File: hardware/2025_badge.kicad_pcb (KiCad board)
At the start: 2 copper layers, 83.8 x 138 mm, 233 parts, among them J1 Conn_01x02, J10 Conn_01x02, J11 Conn_01x02, J12 Conn_01x02, J13 Conn_01x02, J14 Conn_01x02, J15 Conn_01x02, J16 Conn_01x02, J2 Conn_01x02, J3 Conn_01x02, J4 Conn_01x02, J5 Conn_01x02, J6 Conn_01x02, J7 Conn_01x02, J8 Conn_01x02, J9 Conn_01x02, Q1 2N7000, SW1 SW_SPDT, SW2 SW_Push, SW3 SW_Push, U1 TSOP4838

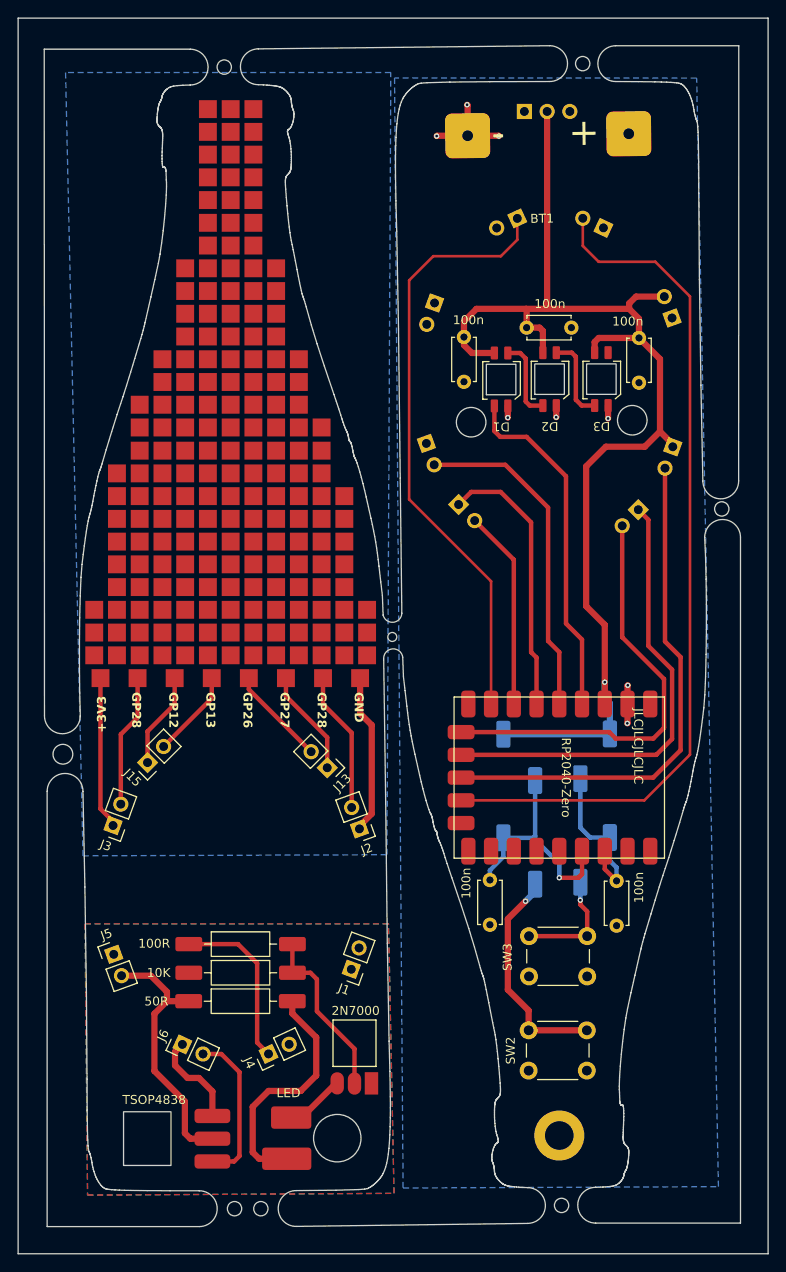
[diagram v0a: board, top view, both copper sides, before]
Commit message: added protection diode and prototype area
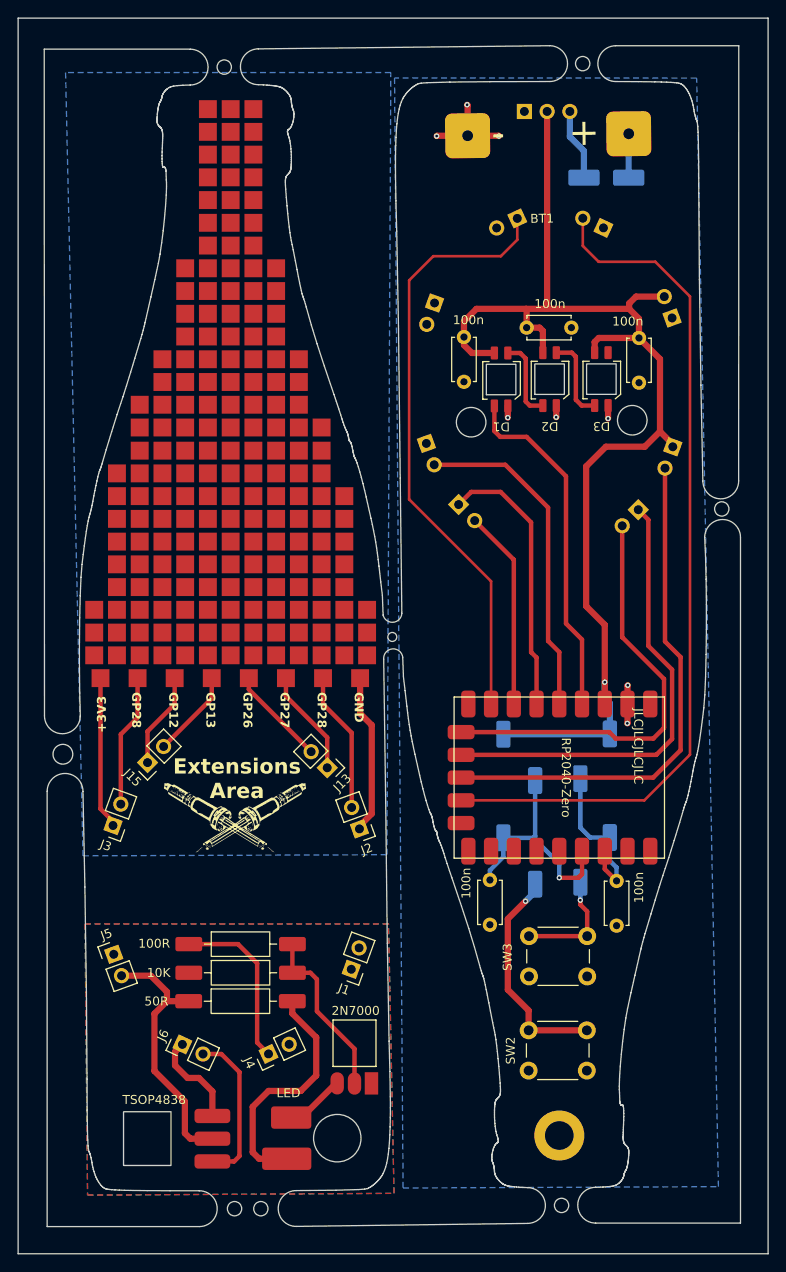
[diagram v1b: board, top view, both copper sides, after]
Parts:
- added D5: D, Diode_SMD:D_SMA_Handsoldering, B.Cu at (103.0, 45.0)
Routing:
- net Net-(D5-K): track 0.00 -> 8.05 mm
- net +BATT: track 0.00 -> 4.91 mm
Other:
- board text added: "Circuit + PCB Design by"
- board text added: "Extensions Area"
- board text added: "RP2040-Zero connections: IR-Tx: GPIO15 IR-Rx: GPIO10 Neopixel: GPIO29"
- board text added: "thx to Friedrich, Matze + all LötBar Guests"
- board text removed: "RP2040-Zero connections: IR-Tx: GPIO13 IR-Rx: GPIO28 Neopixel: GPIO27"

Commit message: fixed wrong IR receiver pinout and footprint
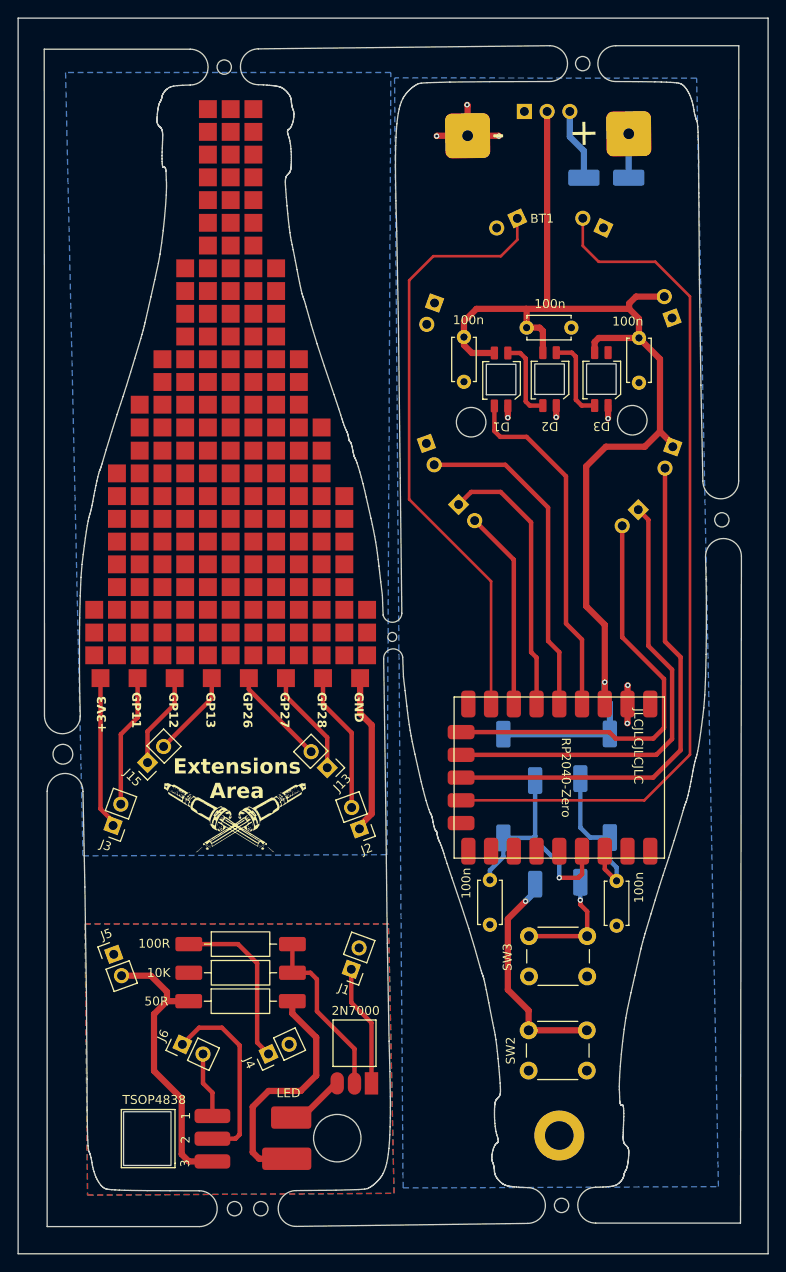
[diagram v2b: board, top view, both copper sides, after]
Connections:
- U1 pad 2: +3V3_bottle -> GND
- U1 pad 3: GND -> +3V3_bottle
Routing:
- net GND: track 10.8 -> 34.9 mm
- net /IR_Rx_bottle: track 17.6 -> 7.35 mm
- net +3V3_bottle: track 29.4 -> 32.0 mm
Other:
- outline, holes or cut-outs redrawn
- board text added: "GP11"
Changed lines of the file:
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@@
 			)
 		)
-		(property "Datasheet" "http://www.vishay.com/docs/82669/tsop32s40f.pdf"
+		(property "Datasheet" "https://www.vishay.com/docs/82489/tsop322.pdf"
 			(at 0 0 90)
 			(unlocked yes)
@@
 		(sheetfile "2025_badge.kicad_sch")
 		(attr smd)
+		(fp_line
+			(start 6.25 -0.25)
+			(end 6.25 5.75)
+			(stroke
+				(width 0.1)
+				(type default)
+			)
+			(layer "F.SilkS")
+		)
+		(fp_line
+			(start -0.25 -0.25)
+			(end 6.25 -0.25)
+			(stroke
+				(width 0.1)
+				(type default)
+			)
+			(layer "F.SilkS")
+		)
+		(fp_line
+			(start 6.25 5.75)
+			(end 0.25 5.75)
+			(stroke
+				(width 0.1)
+				(type default)
+			)
+			(layer "F.SilkS")
+		)
+		(fp_line
+			(start 0.25 5.75)
+			(end -0.25 5.75)
+			(stroke
+				(width 0.1)
+				(type default)
+			)
+			(layer "F.SilkS")
+		)
+		(fp_line
+			(start -0.25 5.75)
+			(end -0.25 -0.25)
+			(stroke
+				(width 0.1)
+				(type default)
+			)
+			(layer "F.SilkS")
+		)
 		(fp_rect
 			(start 0 0)
@@
 		)
 		(fp_rect
-			(start -0.5 -0.125)
+			(start -0.5 -0.375)
 			(end 6.425 12)
 			(stroke
@@
 			(layer "F.CrtYd")
 		)
+		(fp_text user "1"
+			(at 5.1 7.55 90)
+			(unlocked yes)
+			(layer "F.SilkS")
+			(effects
+				(font
+					(size 1 1)
+					(thickness 0.1)
+				)
+				(justify left bottom)
+			)
+		)
+		(fp_text user "2"
+			(at 2.45 7.5 90)
+			(unlocked yes)
+			(layer "F.SilkS")
+			(effects
+				(font
+					(size 1 1)
+					(thickness 0.1)
+				)
+				(justify left bottom)
+			)
+		)
+		(fp_text user "3"
+			(at -0.2 7.45 90)
+			(unlocked yes)
+			(layer "F.SilkS")
+			(effects
+				(font
+					(size 1 1)
+					(thickness 0.1)
+				)
+				(justify left bottom)
+			)
+		)
 		(fp_text user "${REFERENCE}"
 			(at 2.35 -2.025 90)
@@
 		)
 		(pad "1" smd roundrect
-			(at 0.45 9.925 180)
+			(at 5.53 9.925 180)
 			(size 4 1.6)
 			(layers "F.Cu" "F.Mask" "F.Paste")
@@
 			(layers "F.Cu" "F.Mask" "F.Paste")
 			(roundrect_rratio 0.25)
-			(net 18 "+3V3_bottle")
-			(pinfunction "Vs")
+			(net 10 "GND")
+			(pinfunction "GND")
 			(pintype "power_in")
 		)
 		(pad "3" smd roundrect
-			(at 5.53 9.925 180)
+			(at 0.45 9.925 180)
 			(size 4 1.6)
 			(layers "F.Cu" "F.Mask" "F.Paste")
 			(roundrect_rratio 0.25)
-			(net 10 "GND")
-			(pinfunction "GND")
+			(net 18 "+3V3_bottle")
+			(pinfunction "Vs")
 			(pintype "power_in")
 		)
-		(group ""
-			(members "4c17658e-00d6-4f31-940f-1f6d9b959070" "6c455e62-a0a8-4fc4-a7a3-282fd1ab9f6f"
-				"9221312a-7821-42ca-b6e4-d68c84521122"
-			)
-		)
 		(embedded_fonts no)
 	)
@@
 	(gr_line
 		(start 117.991121 161.775086)
-		(end 117.991121 85.179599)
+		(end 118.094244 87.31)
 		(stroke
 			(width 0.05)
@@
 	)
 	(gr_arc
-		(start 113.991121 85.179599)
-		(mid 115.991121 83.179599)
-		(end 117.991121 85.179599)
+		(start 114.085756 87.308841)
+		(mid 116.09058 85.305756)
+		(end 118.094244 87.31)
 		(stroke
 			(width 0.05)
@@
 	)
 	(gr_line
-		(start 113.991121 85.179599)
-		(end 114.085756 87.308841)
-		(stroke
-			(width 0.05)
-			(type default)
-		)
-		(layer "Edge.Cuts")
-	)
-	(gr_line
 		(start 44.927864 136.041628)
 		(end 44.757513 124.238268)
@@
 	)
 	(gr_circle
-		(center 115.9 82)
-		(end 115.9 81.2)
+		(center 115.91 83.22)
+		(end 115.91 82.42)
 		(stroke
 			(width 0.05)
@@
 		)
 	)
-	(gr_text "GP28"
+	(gr_text "GP11"
 		(at 49.916607 102.45 270)
 		(layer "F.SilkS")
@@
 	)
 	(segment
-		(start 56.226039 145.562108)
-		(end 54.826039 144.162108)
-		(width 0.7)
+		(start 57.512675 139.95)
+		(end 55.649017 141.813658)
+		(width 0.5)
 		(layer "F.Cu")
 		(net 10)
 	)
 	(segment
-		(start 59.001039 149.807108)
-		(end 59.001039 147.062108)
-		(width 0.7)
+		(start 61.582892 152.347108)
+		(end 62.05 151.88)
+		(width 0.5)
 		(layer "F.Cu")
 		(net 10)
 	)
 	(segment
-		(start 59.001039 147.062108)
-		(end 57.501039 145.562108)
-		(width 0.7)
+		(start 60.07 139.95)
+		(end 57.512675 139.95)
+		(width 0.5)
 		(layer "F.Cu")
 		(net 10)
 	)
 	(segment
-		(start 54.826039 144.162108)
-		(end 54.826039 142.636636)
-		(width 0.7)
+		(start 59.001039 152.347108)
+		(end 61.582892 152.347108)
+		(width 0.5)
 		(layer "F.Cu")
 		(net 10)
 	)
 	(segment
-		(start 54.826039 142.636636)
-		(end 55.649017 141.813658)
-		(width 0.7)
+		(start 76.768539 146.167108)
+		(end 76.768539 139.398539)
+		(width 0.5)
 		(layer "F.Cu")
 		(net 10)
 	)
 	(segment
-		(start 57.501039 145.562108)
-		(end 56.226039 145.562108)
-		(width 0.7)
+		(start 62.05 141.93)
+		(end 60.07 139.95)
+		(width 0.5)
+		(layer "F.Cu")
+		(net 10)
+	)
+	(segment
+		(start 76.768539 139.398539)
+		(end 74.514964 137.144964)
+		(width 0.5)
+		(layer "F.Cu")
+		(net 10)
+	)
+	(segment
+		(start 74.514964 137.144964)
+		(end 74.514964 133.423927)
+		(width 0.5)
+		(layer "F.Cu")
+		(net 10)
+	)
+	(segment
+		(start 62.05 151.88)
+		(end 62.05 141.93)
+		(width 0.5)
 		(layer "F.Cu")
 		(net 10)
@@
 	)
 	(segment
-		(start 60.001039 142.887108)
-		(end 57.951039 142.887108)
-		(width 0.5)
-		(layer "F.Cu")
-		(net 17)
-	)
-	(segment
-		(start 61.426039 154.887108)
-		(end 62.026039 154.287108)
-		(width 0.5)
-		(layer "F.Cu")
-		(net 17)
-	)
-	(segment
-		(start 62.026039 144.912108)
-		(end 60.001039 142.887108)
+		(start 59.001039 149.807108)
+		(end 59.001039 147.201039)
 		(width 0.5)
 		(layer "F.Cu")
@@
 	)
 	(segment
-		(start 62.026039 154.287108)
-		(end 62.026039 144.912108)
+		(start 59.001039 147.201039)
+		(end 57.951039 146.151039)
 		(width 0.5)
 		(layer "F.Cu")
@@
 	)
 	(segment
-		(start 59.001039 154.887108)
-		(end 61.426039 154.887108)
+		(start 57.951039 146.151039)
+		(end 57.951039 142.887108)
 		(width 0.5)
 		(layer "F.Cu")
@@
 	)
 	(segment
-		(start 59.001039 152.347108)
-		(end 56.536039 152.347108)
+		(start 55.57 154.09)
+		(end 55.57 147.87)
 		(width 0.7)
 		(layer "F.Cu")
@@
 	)
 	(segment
-		(start 48.851039 134.137108)
-		(end 52.126039 134.137108)
+		(start 56.367108 154.887108)
+		(end 55.57 154.09)
 		(width 0.7)
 		(layer "F.Cu")
@@
 	)
 	(segment
-		(start 53.926039 136.987108)
-		(end 56.351039 136.987108)
+		(start 52.48 138.433147)
+		(end 53.926039 136.987108)
 		(width 0.7)
 		(layer "F.Cu")
@@
 	)
 	(segment
-		(start 52.526039 144.787108)
-		(end 52.526039 138.387108)
+		(start 59.001039 154.887108)
+		(end 56.367108 154.887108)
 		(width 0.7)
 		(layer "F.Cu")
@@
 	)
 	(segment
-		(start 55.926039 148.187108)
-		(end 52.526039 144.787108)
+		(start 48.851039 134.137108)
+		(end 52.126039 134.137108)
 		(width 0.7)
 		(layer "F.Cu")
@@
 	)
 	(segment
-		(start 55.926039 151.737108)
-		(end 55.926039 148.187108)
+		(start 52.48 144.78)
+		(end 52.48 138.433147)
 		(width 0.7)
 		(layer "F.Cu")
@@
 	)
 	(segment
-		(start 53.926039 135.937108)
-		(end 53.926039 136.987108)
+		(start 55.57 147.87)
+		(end 52.48 144.78)
 		(width 0.7)
 		(layer "F.Cu")
@@
 	)
 	(segment
-		(start 52.126039 134.137108)
-		(end 53.926039 135.937108)
+		(start 53.926039 136.987108)
+		(end 56.351039 136.987108)
 		(width 0.7)
 		(layer "F.Cu")
@@
 	)
 	(segment
-		(start 52.526039 138.387108)
+		(start 53.926039 135.937108)
 		(end 53.926039 136.987108)
 		(width 0.7)
@@
 	)
 	(segment
-		(start 56.536039 152.347108)
-		(end 55.926039 151.737108)
+		(start 52.126039 134.137108)
+		(end 53.926039 135.937108)
 		(width 0.7)
 		(layer "F.Cu")

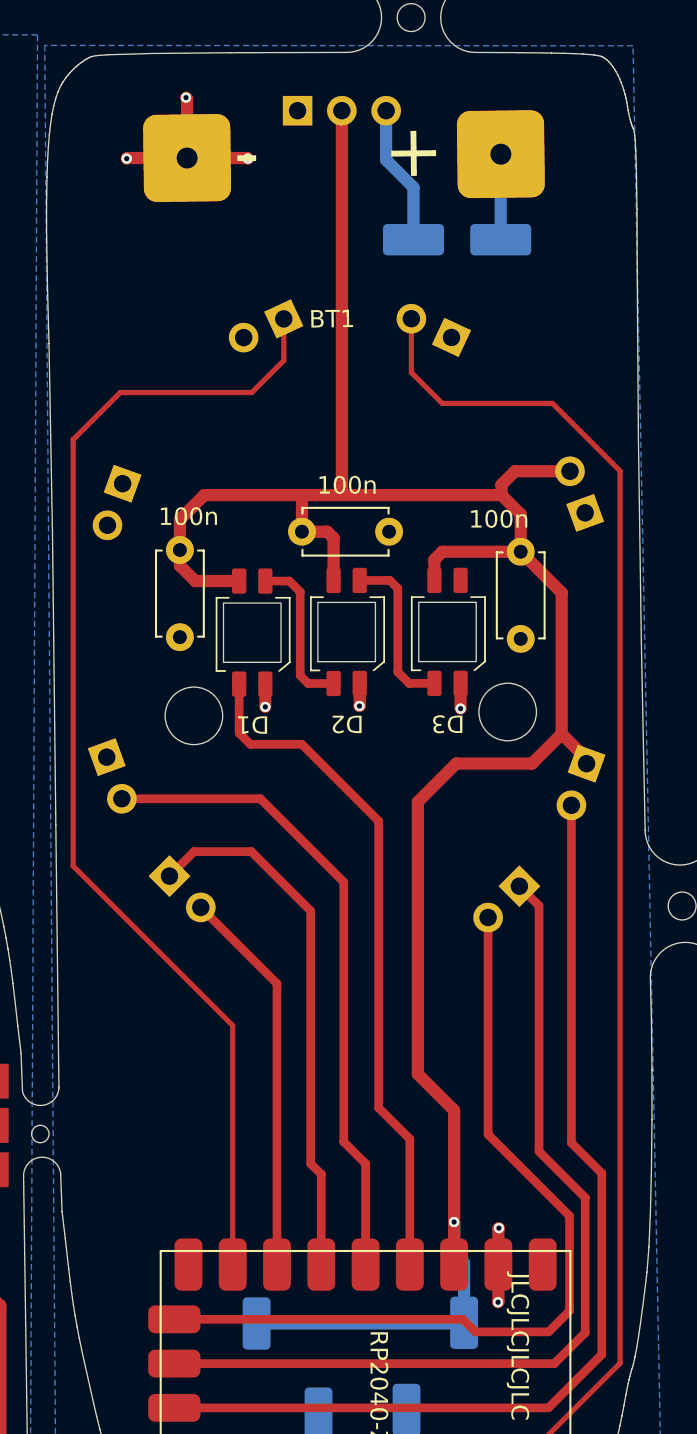
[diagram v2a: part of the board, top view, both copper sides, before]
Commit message: use WS2812B pinout compatible LEDs with easy to solder footprint
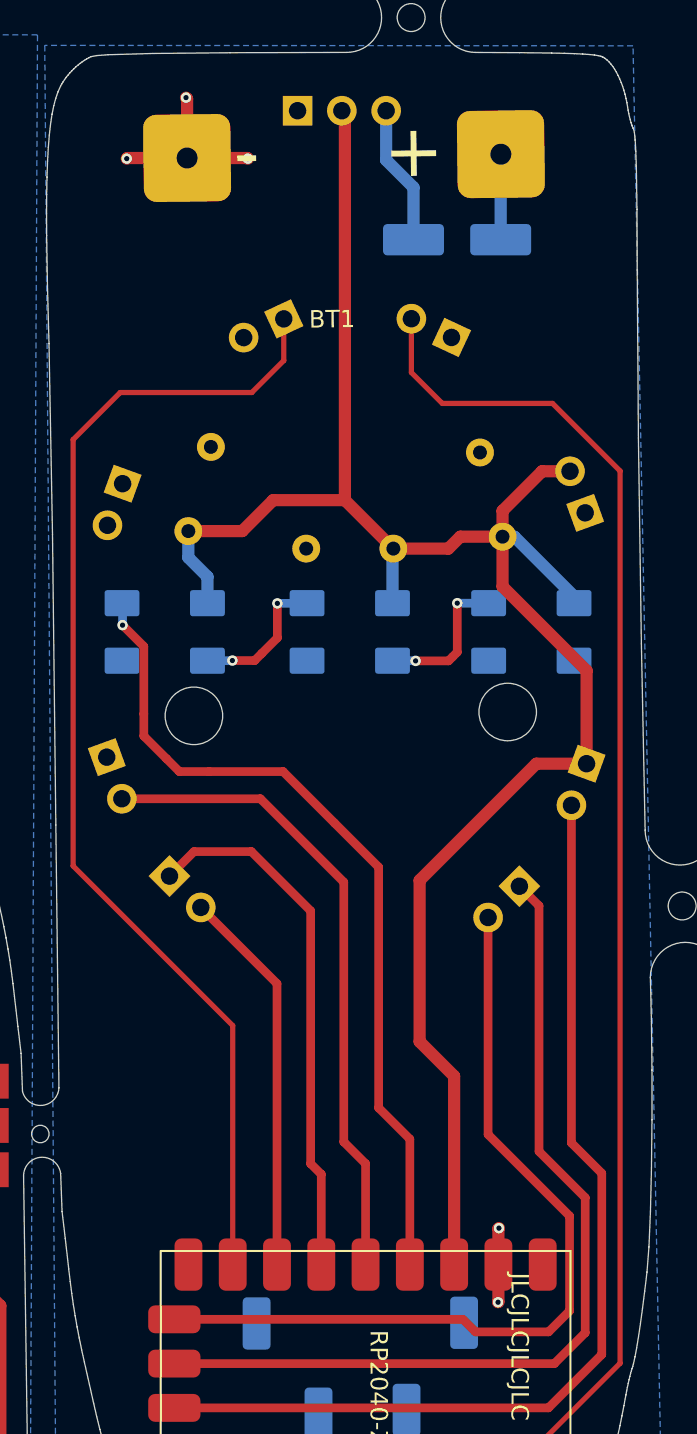
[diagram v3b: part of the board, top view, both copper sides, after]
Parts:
- removed D3: SK6812-E, project_lib:SK6812-E_reverse_mount_neopixel
- added D6: WS2812B, LED_SMD:LED_WS2812B_PLCC4_5.0x5.0mm_P3.2mm, B.Cu at (107.3, 67.5)
- C1, C2, C3: moved to B.Cu
- D1, D2: value SK6812-E -> WS2812B; footprint project_lib:SK6812-E_reverse_mount_neopixel -> LED_SMD:LED_WS2812B_PLCC4_5.0x5.0mm_P3.2mm; moved to B.Cu
- R5, R6: value 10K -> 100R
- moved D2 9.82 mm to (86.2, 67.5), turned to 180 degrees
- moved D1 6.55 mm to (96.8, 67.5), turned to 180 degrees
- moved C2 5.33 mm to (99.3, 62.7), turned to 180 degrees
- moved C3 1.36 mm to (105.6, 62.0), turned to 105 degrees
- moved C1 1.19 mm to (87.6, 61.7), turned to 75 degrees
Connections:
- D1 pad 2: Net-(D1-Dout) -> Net-(D1-DOUT)
- D1 pad 4: /neopixel_D_in -> Net-(D1-DIN)
- D2 pad 2: Net-(D2-Dout) -> Net-(D1-DIN)
- D2 pad 4: Net-(D1-Dout) -> /neopixel_D_in
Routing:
- net +3V3: track 138.4 -> 113.4 mm, vias 1 -> 0
- net Net-(D2-Dout): track 9.54 -> 0.00 mm
- net /neopixel_D_in: track 39.7 -> 48.9 mm, vias 0 -> 1
- net Net-(D1-Dout): track 9.16 -> 0.00 mm
- net Net-(D1-DOUT): track 0.00 -> 8.54 mm, vias 0 -> 2
- net Net-(D1-DIN): track 0.00 -> 8.24 mm, vias 0 -> 2
- net GND1: track 18.8 -> 14.7 mm, vias 8 -> 5
